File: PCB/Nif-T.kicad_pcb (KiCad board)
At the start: 2 copper layers, 100 x 100 mm, 0 parts

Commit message: PCB Reconfigured and Rerouted
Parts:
- added BUZZER1: FST-1230, imported_components:BUZ-SMD_L12.0-W12.0_FUET-1230, F.Cu at (233.2, 142.2)
- added C1: 0.22uF, imported_components:C0805, F.Cu at (173.8, 74.6)
- added C10: 0.1uF, imported_components:C0805, F.Cu at (239.4, 94.4)
- added C11: 1uF, imported_components:C0805, F.Cu at (243.0, 62.6)
- added C12: 10uF, imported_components:C0805, F.Cu at (236.6, 57.8)
- added C13: 0.1uF, imported_components:C0805, F.Cu at (240.8, 57.8)
- added C14: 10uF, imported_components:C0805, F.Cu at (204.2, 61.8)
- added C15: RVT1H470M0607, imported_components:CAP-SMD_BD6.3-L6.6-W6.6-LS7.6-FD, F.Cu at (219.4, 69.1)
- added C16: 10uF, imported_components:C0805, F.Cu at (214.4, 78.8)
- added C17: 10uF, imported_components:C0805, F.Cu at (204.2, 59.6)
- added C18: 10uF, imported_components:C0805, F.Cu at (214.4, 85.2)
- added C19: RVT1E331M0810, imported_components:CAP-SMD_BD8.0-L8.3-W8.3-LS9.3-FD-1, F.Cu at (198.8, 86.6)
- added C2: 0.22uF, imported_components:C0805, F.Cu at (169.0, 87.6)
- added C20: 0.1uF, imported_components:C0805, F.Cu at (239.4, 98.4)
- added C3: 0.22uF, imported_components:C0805, F.Cu at (172.4, 92.0)
- added C4: 0.1uF, imported_components:C0805, F.Cu at (220.2, 84.8)
- added C5: 0.1uF, imported_components:C0805, F.Cu at (175.3, 82.9)
- added C6: 1uF, imported_components:C0805, F.Cu at (172.0, 82.9)
- added C7: 0.1uF, imported_components:C0805, F.Cu at (182.8, 82.1)
- added C8: 1uF, imported_components:C0805, F.Cu at (186.0, 80.1)
- added C9: 0.1uF, imported_components:C0805, F.Cu at (239.4, 90.4)
- added D1: SS54_C22452, imported_components:SMA_L4.4-W2.8-LS5.4-R-RD, F.Cu at (157.2, 83.0)
- added D10: SK6812, LED_SMD:LED_SK6812_PLCC4_5.0x5.0mm_P3.2mm, F.Cu at (197.6, 121.7)
- added D11: SK6812, LED_SMD:LED_SK6812_PLCC4_5.0x5.0mm_P3.2mm, F.Cu at (197.6, 129.8)
- added D12: SK6812, LED_SMD:LED_SK6812_PLCC4_5.0x5.0mm_P3.2mm, F.Cu at (197.6, 137.8)
- added D13: SK6812, LED_SMD:LED_SK6812_PLCC4_5.0x5.0mm_P3.2mm, F.Cu at (203.2, 137.8)
- added D14: 1N4148W-E3-08, new_imported_components:SOD-123_L2.8-W1.8-LS3.7-RD, F.Cu at (225.1, 118.0)
- added D15: 1N4148W-E3-08, new_imported_components:SOD-123_L2.8-W1.8-LS3.7-RD, F.Cu at (217.0, 118.0)
- added D16: 1N4148W-E3-08, new_imported_components:SOD-123_L2.8-W1.8-LS3.7-RD, F.Cu at (224.4, 144.2)
- added D17: 1N4148W-E3-08, new_imported_components:SOD-123_L2.8-W1.8-LS3.7-RD, F.Cu at (216.4, 144.2)
- added D18: 1N4148W-E3-08, new_imported_components:SOD-123_L2.8-W1.8-LS3.7-RD, F.Cu at (175.3, 110.0)
- added D19: 1N4148W-E3-08, new_imported_components:SOD-123_L2.8-W1.8-LS3.7-RD, F.Cu at (183.1, 110.0)
- added D2: SS54_C22452, imported_components:SMA_L4.4-W2.8-LS5.4-R-RD, F.Cu at (200.4, 79.0)
- added D20: 1N4148W-E3-08, new_imported_components:SOD-123_L2.8-W1.8-LS3.7-RD, F.Cu at (197.2, 142.4)
- added D21: 1N4148W-E3-08, new_imported_components:SOD-123_L2.8-W1.8-LS3.7-RD, F.Cu at (197.2, 144.4)
- added D22: SS54_C22452, imported_components:SMA_L4.4-W2.8-LS5.4-R-RD, F.Cu at (214.6, 72.4)
- added D3: LED, imported_components:LED0805-RD, F.Cu at (217.8, 81.8)
- added D4: SK6812, LED_SMD:LED_SK6812_PLCC4_5.0x5.0mm_P3.2mm, F.Cu at (203.2, 113.6)
- added D5: SK6812, LED_SMD:LED_SK6812_PLCC4_5.0x5.0mm_P3.2mm, F.Cu at (203.2, 105.6)
- added D6: SK6812, LED_SMD:LED_SK6812_PLCC4_5.0x5.0mm_P3.2mm, F.Cu at (203.2, 121.7)
- added D7: SK6812, LED_SMD:LED_SK6812_PLCC4_5.0x5.0mm_P3.2mm, F.Cu at (203.2, 129.8)
- added D8: SK6812, LED_SMD:LED_SK6812_PLCC4_5.0x5.0mm_P3.2mm, F.Cu at (197.6, 105.6)
- added D9: SK6812, LED_SMD:LED_SK6812_PLCC4_5.0x5.0mm_P3.2mm, F.Cu at (197.6, 113.6)
- added H1: MountingHole, MountingHole:MountingHole_3.2mm_M3_Pad_Via, F.Cu at (154.4, 54.4)
- added H2: MountingHole, MountingHole:MountingHole_3.2mm_M3_Pad_Via, F.Cu at (245.5, 54.5)
- added H3: MountingHole, MountingHole:MountingHole_3.2mm_M3_Pad_Via, F.Cu at (154.4, 145.6)
- added H4: MountingHole, MountingHole:MountingHole_3.2mm_M3_Pad_Via, F.Cu at (245.6, 145.6)
- added J1: Barrel_Jack, imported_components:DC-IN-TH_DC-005-A200, F.Cu at (213.3, 60.8)
- added J2: Conn_01x02, imported_components:CONN-TH_P5.00_KF301-5.0-2P, F.Cu at (226.3, 54.0)
- added J3: Conn_02x03_Odd_Even, imported_components:HDR-SMD_6P-P2.54-V, F.Cu at (162.2, 99.0)
- added J4: Conn_02x03_Odd_Even, imported_components:HDR-SMD_6P-P2.54-V, F.Cu at (172.6, 99.0)
- added J5: Conn_02x03_Odd_Even, imported_components:HDR-SMD_6P-P2.54-V, F.Cu at (182.8, 99.0)
- added J6: Conn_02x03_Odd_Even, imported_components:HDR-SMD_6P-P2.54-V, F.Cu at (193.1, 99.0)
- added J7: Conn_02x03_Odd_Even, imported_components:HDR-SMD_6P-P2.54-V, F.Cu at (203.3, 99.0)
- added L1: CYA1040-33UH, imported_components:IND-SMD_L11.6-W10.1, F.Cu at (208.0, 70.4)
- added L2: BLM21PG221SN1D, new_imported_components:L0805, F.Cu at (190.4, 80.0)
- added P1: USB_C_Plug, imported_components:USB-C_SMD-TYPE-C-31-M-12, F.Cu at (196.4, 55.5)
- added Q1: S8050, new_imported_components:SOT-23-3_L2.9-W1.3-P1.90-LS2.4-BR, F.Cu at (211.2, 104.4)
- added Q2: S8050, new_imported_components:SOT-23-3_L2.9-W1.3-P1.90-LS2.4-BR, F.Cu at (213.2, 107.6)
- added Q3: S8050, new_imported_components:SOT-23-3_L2.9-W1.3-P1.90-LS2.4-BR, F.Cu at (215.8, 104.4)
- added Q4: S8050, new_imported_components:SOT-23-3_L2.9-W1.3-P1.90-LS2.4-BR, F.Cu at (217.8, 107.6)
- added Q5: S8050, new_imported_components:SOT-23-3_L2.9-W1.3-P1.90-LS2.4-BR, F.Cu at (220.4, 104.4)
- added Q6: S8050, new_imported_components:SOT-23-3_L2.9-W1.3-P1.90-LS2.4-BR, F.Cu at (222.4, 107.4)
- added Q7: S8050, new_imported_components:SOT-23-3_L2.9-W1.3-P1.90-LS2.4-BR, F.Cu at (225.0, 104.5)
- added Q8: S8050, new_imported_components:SOT-23-3_L2.9-W1.3-P1.90-LS2.4-BR, F.Cu at (227.0, 107.6)
- added R1: 12.1k, imported_components:R0805, F.Cu at (173.6, 78.4)
- added R10: 10k, imported_components:R0805, F.Cu at (236.0, 90.4)
- added R11: 10k, imported_components:R0805, F.Cu at (236.0, 94.4)
- added R12: 10k, imported_components:R0805, F.Cu at (240.0, 61.6)
- added R13: 10k, imported_components:R0805, F.Cu at (240.0, 63.8)
- added R14: 200, imported_components:R0805, F.Cu at (219.0, 75.9)
- added R15: 10k, imported_components:R0805, F.Cu at (236.0, 98.4)
- added R2: 22, imported_components:R0805, F.Cu at (186.4, 87.4)
- added R3: 10k, imported_components:R0805, F.Cu at (221.2, 80.8)
- added R4: 49.9, imported_components:R0805, F.Cu at (177.2, 74.4)
- added R5: 49.9, imported_components:R0805, F.Cu at (180.6, 74.4)
- added R6: 49.9, imported_components:R0805, F.Cu at (187.4, 74.4)
- added R7: 49.9, imported_components:R0805, F.Cu at (184.0, 74.4)
- added R8: 5.1k, imported_components:R0805, F.Cu at (204.2, 52.8)
- added R9: 5.1k, imported_components:R0805, F.Cu at (204.2, 56.2)
- added RJ1: HY931147C, new_imported_components:RJ45-TH_HY931147C, F.Cu at (181.7, 63.5)
- added RLY1: G5NB-1A-E-DC5V, new_imported_components:RELAY-TH_G5NB-1A-E-DCXX, F.Cu at (216.7, 113.2)
- added RLY2: G5NB-1A-E-DC5V, new_imported_components:RELAY-TH_G5NB-1A-E-DCXX, F.Cu at (216.7, 122.8)
- added RLY3: G5NB-1A-E-DC5V, new_imported_components:RELAY-TH_G5NB-1A-E-DCXX, F.Cu at (216.6, 131.4)
- added RLY4: G5NB-1A-E-DC5V, new_imported_components:RELAY-TH_G5NB-1A-E-DCXX, F.Cu at (216.6, 139.4)
- added RLY5: G5NB-1A-E-DC5V, new_imported_components:RELAY-TH_G5NB-1A-E-DCXX, F.Cu at (183.2, 105.4)
- added RLY6: G5NB-1A-E-DC5V, new_imported_components:RELAY-TH_G5NB-1A-E-DCXX, F.Cu at (183.2, 114.8)
- added RLY7: G5NB-1A-E-DC5V, new_imported_components:RELAY-TH_G5NB-1A-E-DCXX, F.Cu at (183.2, 123.7)
- added RLY8: G5NB-1A-E-DC5V, new_imported_components:RELAY-TH_G5NB-1A-E-DCXX, F.Cu at (191.2, 138.2)
- added SW1: SW_Push, imported_components:SW-SMD_L3.9-W3.0-P4.45, F.Cu at (246.8, 89.8)
- added SW2: SW_Push, imported_components:SW-SMD_L3.9-W3.0-P4.45, F.Cu at (246.8, 93.0)
- added SW3: SW_Push, imported_components:SW-SMD_L3.9-W3.0-P4.45, F.Cu at (246.8, 96.2)
- added SW4: SW_SPDT, imported_components:SW-SMD_MST-12D18G4-SPDT-SLIDE-SWITCH, F.Cu at (236.6, 55.4)
- added SW5: DSIC-05-LS-GER, new_imported_components:SW-SMD_DSIC-05-LS-GER, F.Cu at (228.0, 95.6)
- added SW6: DSIC-05-LS-GER, new_imported_components:SW-SMD_DSIC-05-LS-GER, F.Cu at (215.3, 95.6)
- added U1: ESP32-WROOM-32E(4MB), new_imported_components:WIFI-SMD_ESP32-WROOM-32E, F.Cu at (233.3, 76.5)
- added U10: DB128B-5.08-3P-BK-S, new_imported_components:CONN-TH_DB128B-5.08-3P-XX-S, F.Cu at (162.6, 129.0)
- added U11: DB128B-5.08-3P-BK-S, new_imported_components:CONN-TH_DB128B-5.08-3P-XX-S, F.Cu at (178.6, 137.4)
- added U2: LAN8720A-CP-TR, new_imported_components:QFN-24_L4.0-W4.0-P0.50-BL-EP2.6, F.Cu at (179.7, 85.5)
- added U3: DP1435-5V, new_imported_components:PWRM-TH_DP1435-XX, F.Cu at (162.4, 68.4)
- added U4: CH340C, Package_SO:SOIC-16_3.9x9.9mm_P1.27mm, F.Cu at (228.8, 62.1)
- added U5: LM2596SX-5.0/NOPB, imported_components:TO-263-5_L10.2-W8.9-P1.70-TL, F.Cu at (196.4, 67.6)
- added U6: AMS1117-3.3, Package_TO_SOT_SMD:SOT-223-3_TabPin2, F.Cu at (208.6, 81.8)
- added U7: DB128B-5.08-3P-BK-S, new_imported_components:CONN-TH_DB128B-5.08-3P-XX-S, F.Cu at (237.2, 111.2)
- added U8: DB128B-5.08-3P-BK-S, new_imported_components:CONN-TH_DB128B-5.08-3P-XX-S, F.Cu at (237.2, 129.4)
- added U9: DB128B-5.08-3P-BK-S, new_imported_components:CONN-TH_DB128B-5.08-3P-XX-S, F.Cu at (162.6, 110.8)
- added X1: X322525MOB4SI, new_imported_components:CRYSTAL-SMD_4P-L3.2-W2.5-BL, F.Cu at (174.2, 87.3)
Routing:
- net +5V: track 0.00 -> 529.0 mm
- net GPIO 33: track 0.00 -> 181.4 mm, vias 0 -> 2
- net GPIO 32: track 0.00 -> 181.1 mm, vias 0 -> 2
- net GPIO 37: track 0.00 -> 180.0 mm, vias 0 -> 2
- net GPIO 35: track 0.00 -> 179.7 mm, vias 0 -> 4
- net GPIO 36: track 0.00 -> 168.5 mm, vias 0 -> 2
- net +3.3V: track 0.00 -> 128.2 mm, vias 0 -> 6
- net Net-(D20-A): track 0.00 -> 106.0 mm, vias 0 -> 4
- net 8720RST: track 0.00 -> 89.9 mm, vias 0 -> 4
- net RXD0/MODE0: track 0.00 -> 86.6 mm, vias 0 -> 2
- net RXD1/MODE1: track 0.00 -> 86.6 mm, vias 0 -> 2
- net Net-(D16-A): track 0.00 -> 84.9 mm, vias 0 -> 5
- net Net-(D21-A): track 0.00 -> 83.4 mm, vias 0 -> 2
- net CRS_DV/MODE2: track 0.00 -> 83.1 mm, vias 0 -> 2
- net ETH_CLK: track 0.00 -> 78.8 mm, vias 0 -> 2
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- added copper zone on B.Cu, net GND
- added copper zone on F.Cu, net GND
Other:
- outline, holes or cut-outs redrawn
- board text added: "USR"

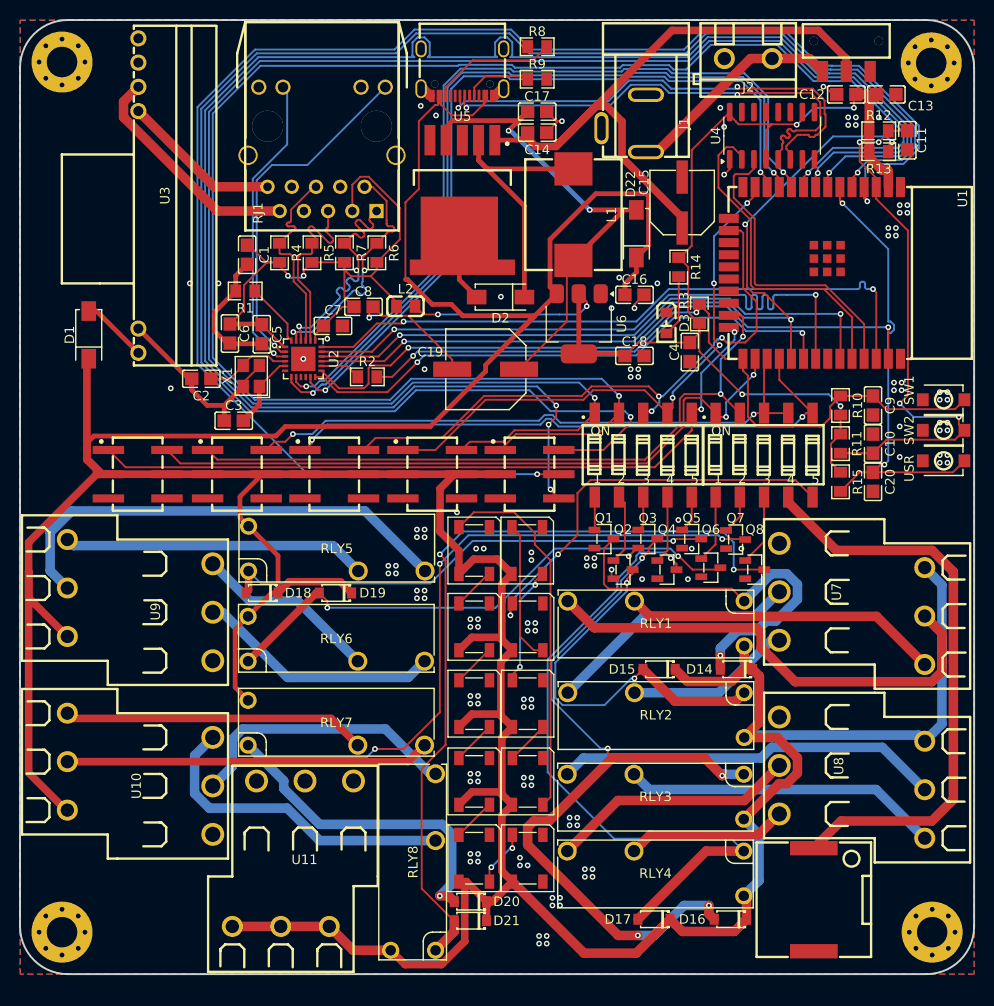
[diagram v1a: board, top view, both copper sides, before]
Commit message: Add Nif-T ESP32 firmware
Added initial Nif-T_firmware.ino for ESP32-WROOM-32E with LAN8720A Ethernet, MQTT relay/LED control, and Home Assistant discovery.
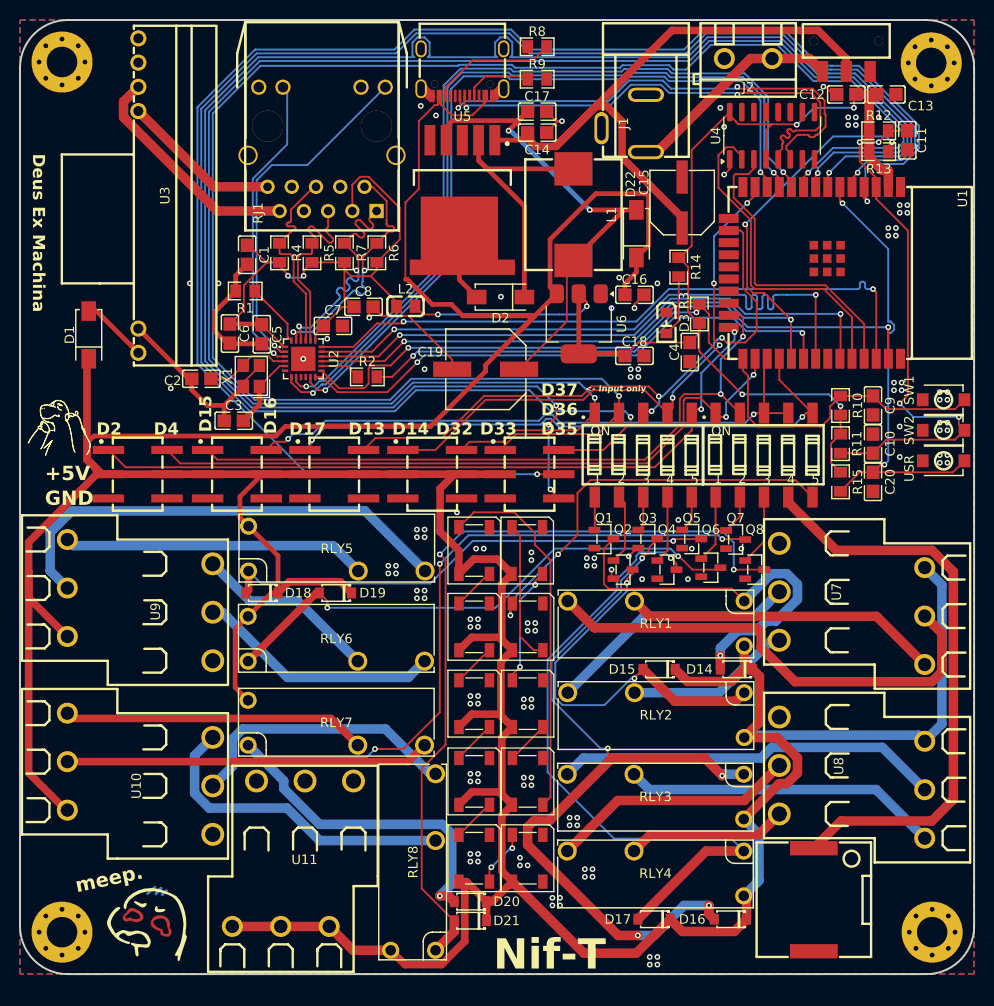
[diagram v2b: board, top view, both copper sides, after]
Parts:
- added G***: LOGO, LOGO, F.Cu at (163.4, 144.6)
- added G***: LOGO, LOGO, F.Cu at (154.2, 92.8)
- added G***: LOGO, LOGO, B.Cu at (171.0, 69.2)
- added G***: LOGO, LOGO, B.Cu at (196.2, 94.6)
- added G***: LOGO, LOGO, B.Cu at (165.2, 141.2)
- added G***: LOGO, LOGO, B.Cu at (222.0, 76.3)
- added G***: LOGO, LOGO, B.Cu at (172.6, 107.8)
- added G***: LOGO, LOGO, B.Cu at (219.7, 124.0)
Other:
- board text added: "+5V"
- board text added: "<- Input only"
- board text added: "D13"
- board text added: "D14"
- board text added: "D15"
- board text added: "D16"
- board text added: "D17"
- board text added: "D2"
- board text added: "D32"
- board text added: "D33"
- board text added: "D37 D36 D35"
- board text added: "D4"
- board text added: "Deus Ex Machina"
- board text added: "GND"
- board text added: "Logan Peterson"
- board text added: "Nif-T"
- board text added: "USB-SEE"
- board text added: "meep."
